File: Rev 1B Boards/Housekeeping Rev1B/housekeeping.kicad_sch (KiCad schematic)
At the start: 41 parts, among them U14 MC34063A, U15 MC34063A, U16 TPS54302

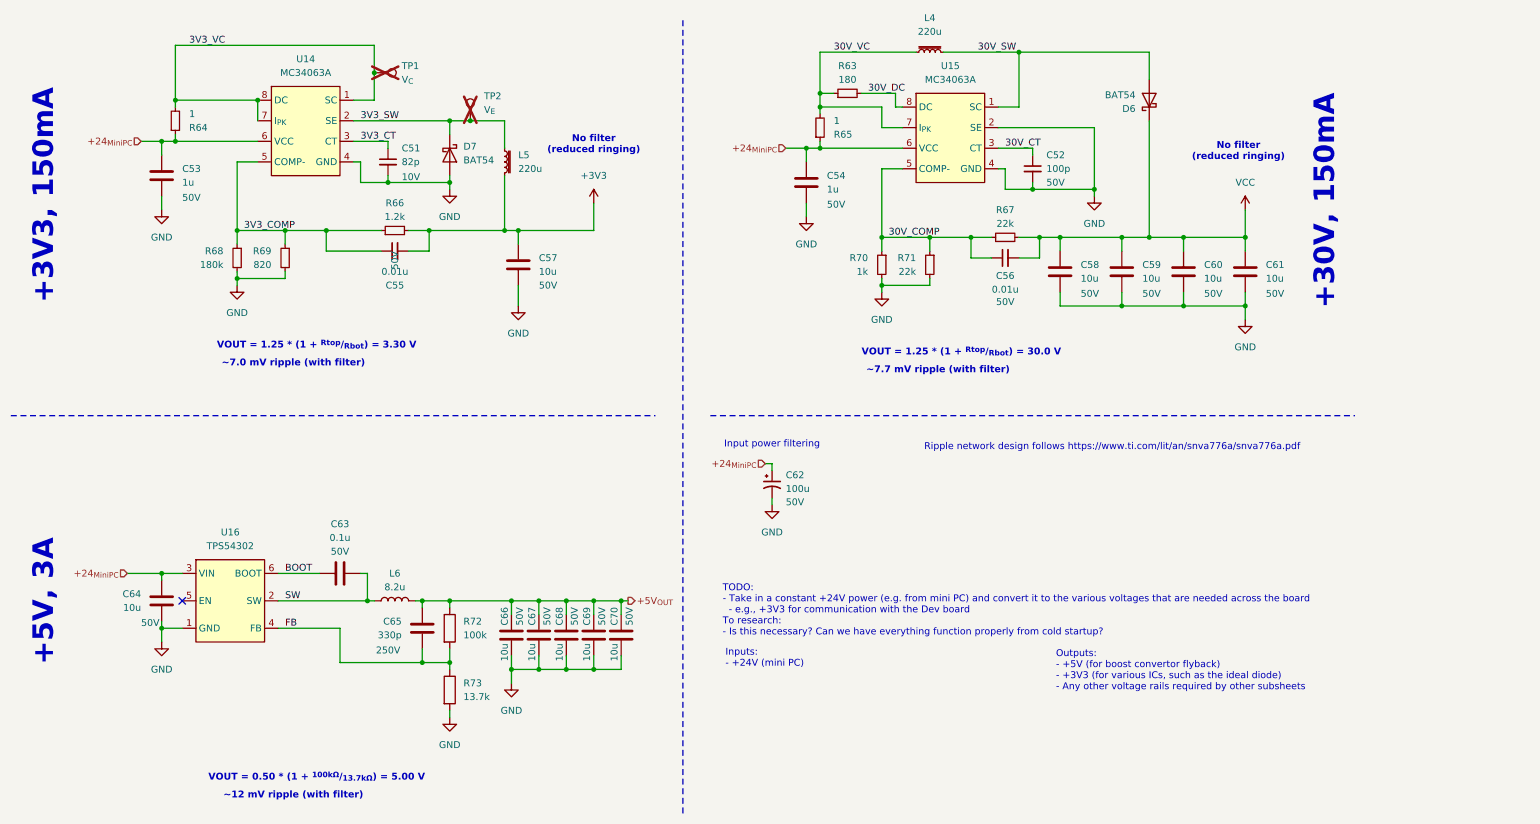
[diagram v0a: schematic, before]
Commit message: Specc'd all components + started creating rev 1b boards
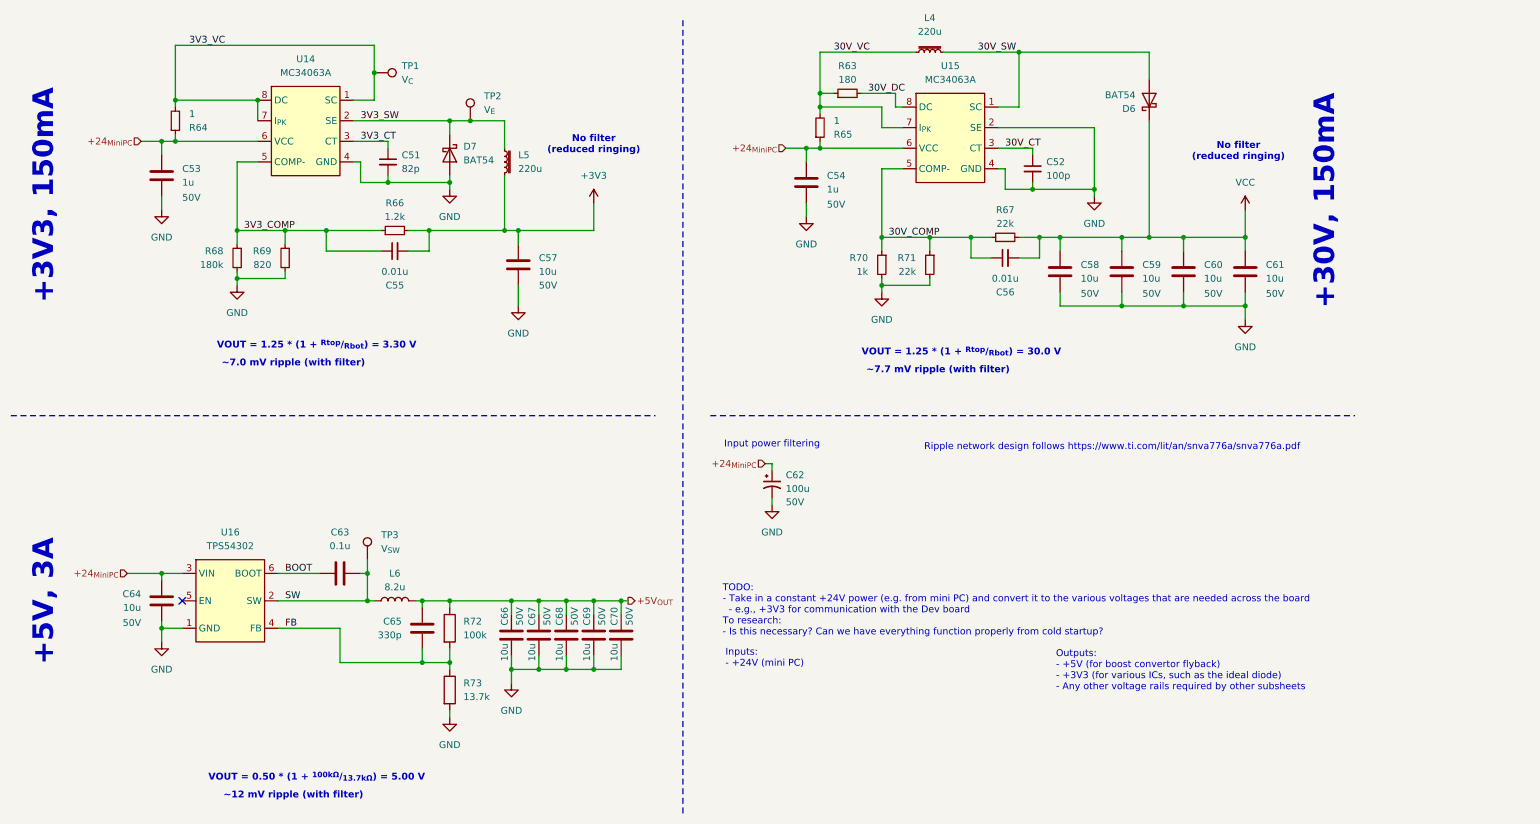
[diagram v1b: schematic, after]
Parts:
- added TP3: V_{SW}, TestPoint:TestPoint_Bridge_Pitch2.0mm_Drill0.7mm, symbol Connector:TestPoint
- C51: Mouser Part Number 791-0603N820J100CT -> (none); Voltage Rating 10V -> (none)
- C52: Mouser Part Number 77-VJ0603A101KXACBC -> (none); Voltage Rating 50V -> (none)
- C55, C56: Mouser Part Number 187-CL10B103KC8NNNC -> (none); Voltage Rating 50V -> (none)
- C63: Mouser Part Number 581-KGM15BR71H104JT -> (none); Voltage Rating 50V -> (none)
- C65: Mouser Part Number 791-0805N331J251CT -> (none); Voltage Rating 250V -> (none)
- R63: footprint Resistor_SMD:R_0805_2012Metric_Pad1.20x1.40mm_HandSolder -> Resistor_SMD:R_0603_1608Metric_Pad0.98x0.95mm_HandSolder; Mouser Part Number 667-ERJ-P06J181V -> (none)
- R66: Mouser Part Number 603-RT0603DRD071K2L -> 603-RT0603FRE133K6L
- R67, R71: Mouser Part Number 71-CRCW0603-22K-E3 -> (none)
- R68: Mouser Part Number 603-RT0603DRE07180KL -> (none)
- R69: Mouser Part Number 667-ERA-3AEB821V -> (none)
- R70: Mouser Part Number 660-RN73R1JTD1001F50 -> 755-ESR03EZPJ222
- R72: Mouser Part Number 660-RN73H1JTD1003D25 -> (none)
- R73: Mouser Part Number 603-AC0603FR-0713K7L -> (none)
- TP1, TP2: now fitted
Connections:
- net SW: now also TP3.1
